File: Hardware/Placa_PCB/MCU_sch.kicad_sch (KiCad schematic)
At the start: 22 parts, among them J10 Conn_01x09_Pin, J9 Conn_01x09_Pin, U4 MIC29302AWD, U5 ESP32-S3-WROOM-1

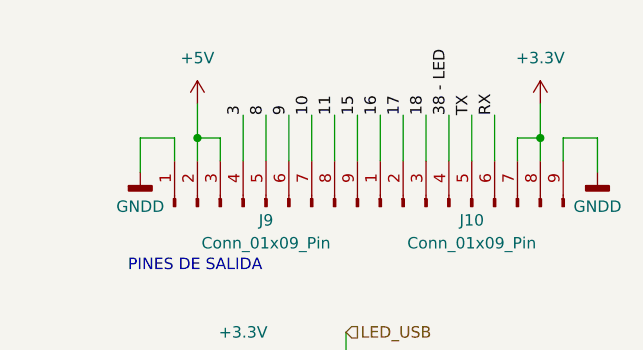
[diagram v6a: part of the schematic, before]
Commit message: Actualizacion de PCB con rellenos ordenados, solo falta colocar las vias
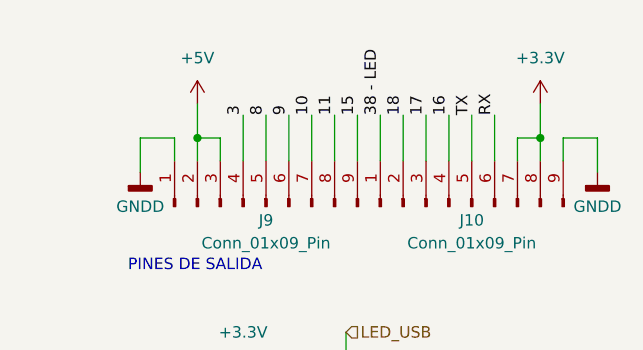
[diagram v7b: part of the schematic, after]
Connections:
- net 16: now also J10.4 (Pin_4); no longer J10.1 (Pin_1)
- net 17: now also J10.3 (Pin_3); no longer J10.2 (Pin_2)
- net 18: now also J10.2 (Pin_2); no longer J10.3 (Pin_3)
- net 38 - LED: now also J10.1 (Pin_1); no longer J10.4 (Pin_4)
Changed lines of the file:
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@@
 	)
 	(label "16"
-		(at 231.14 71.12 90)
+		(at 238.76 71.12 90)
 		(effects
 			(font
@@
 	)
 	(label "17"
-		(at 233.68 71.12 90)
+		(at 236.22 71.12 90)
 		(effects
 			(font
@@
 	)
 	(label "38 - LED"
-		(at 238.76 71.12 90)
+		(at 231.14 71.12 90)
 		(effects
 			(font
@@
 	)
 	(label "18"
-		(at 236.22 71.12 90)
+		(at 233.68 71.12 90)
 		(effects
 			(font
